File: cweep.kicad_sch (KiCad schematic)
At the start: 57 parts

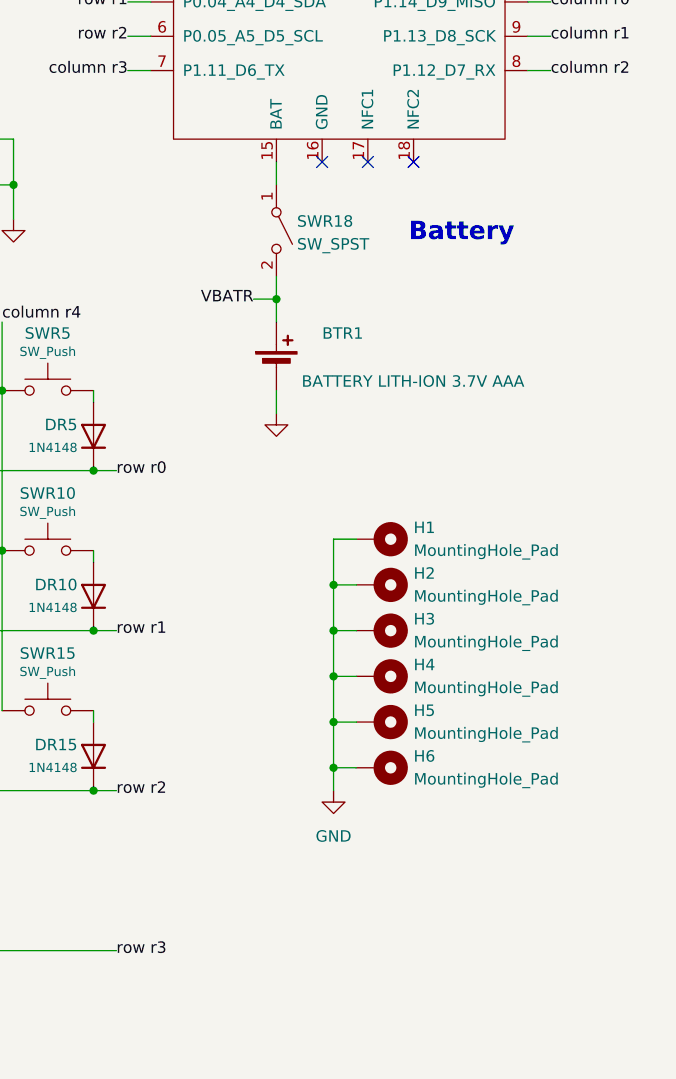
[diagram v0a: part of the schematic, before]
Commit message: refactor: reorganize battery schematic
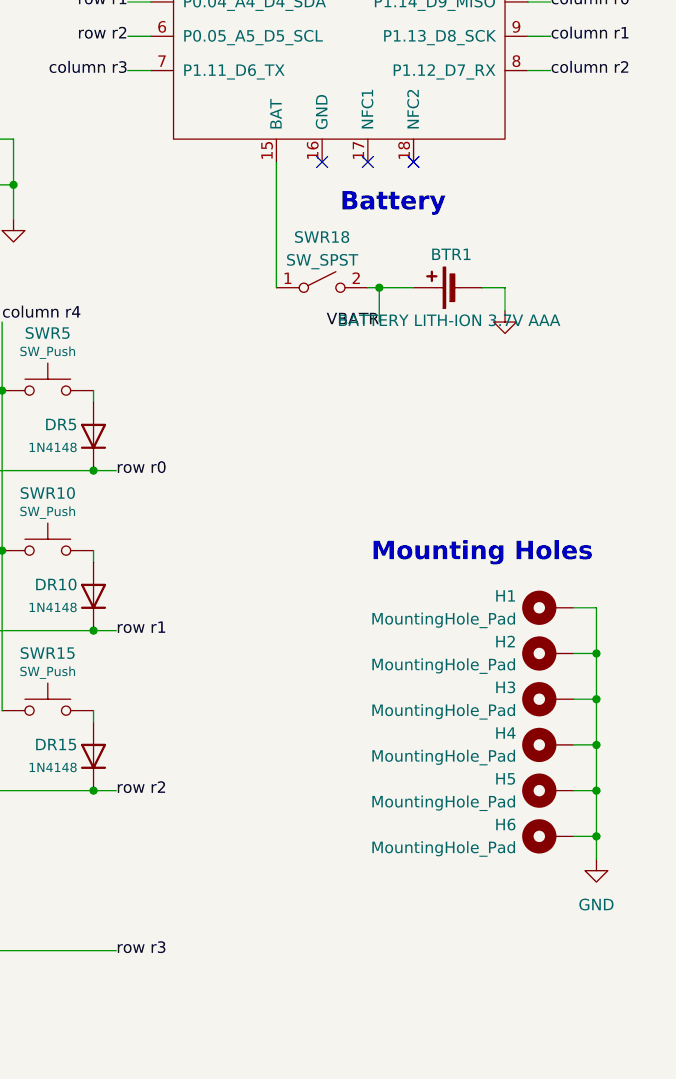
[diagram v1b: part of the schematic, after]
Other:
- note added: "Mounting Holes"
- moved on the sheet: BTR1, H1, H2, H3, H4, H5, H6, SWR18

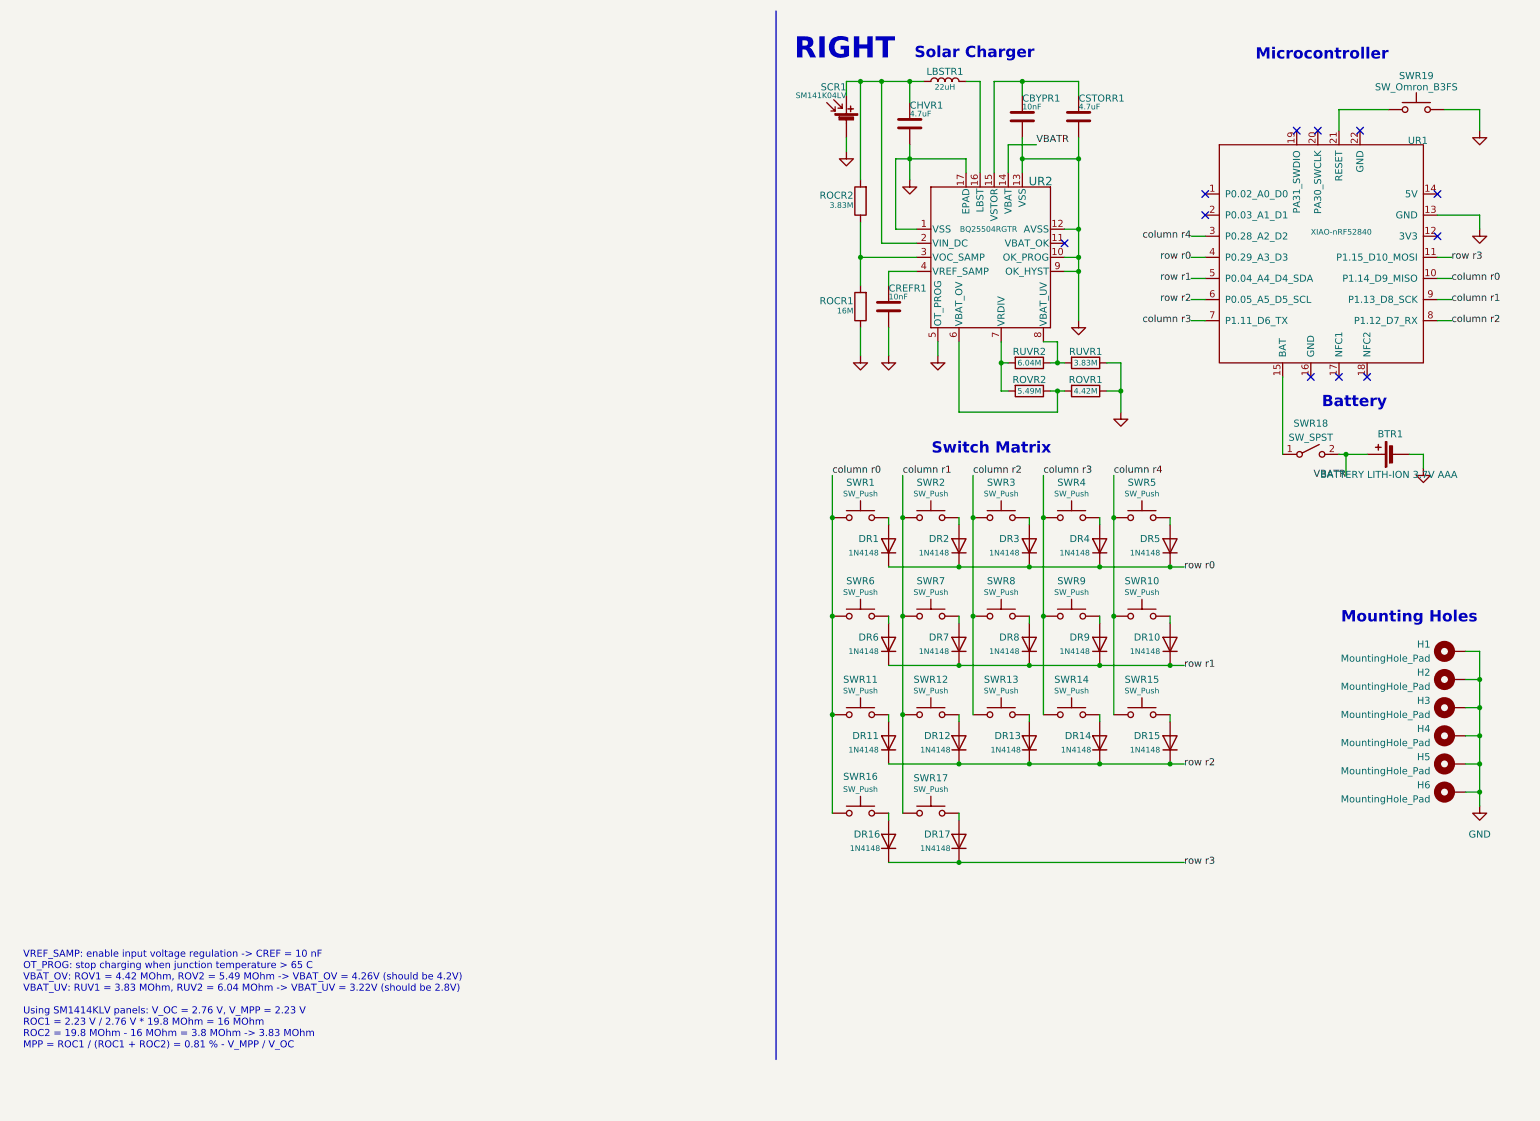
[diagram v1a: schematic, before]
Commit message: feat: add solar cell connectors
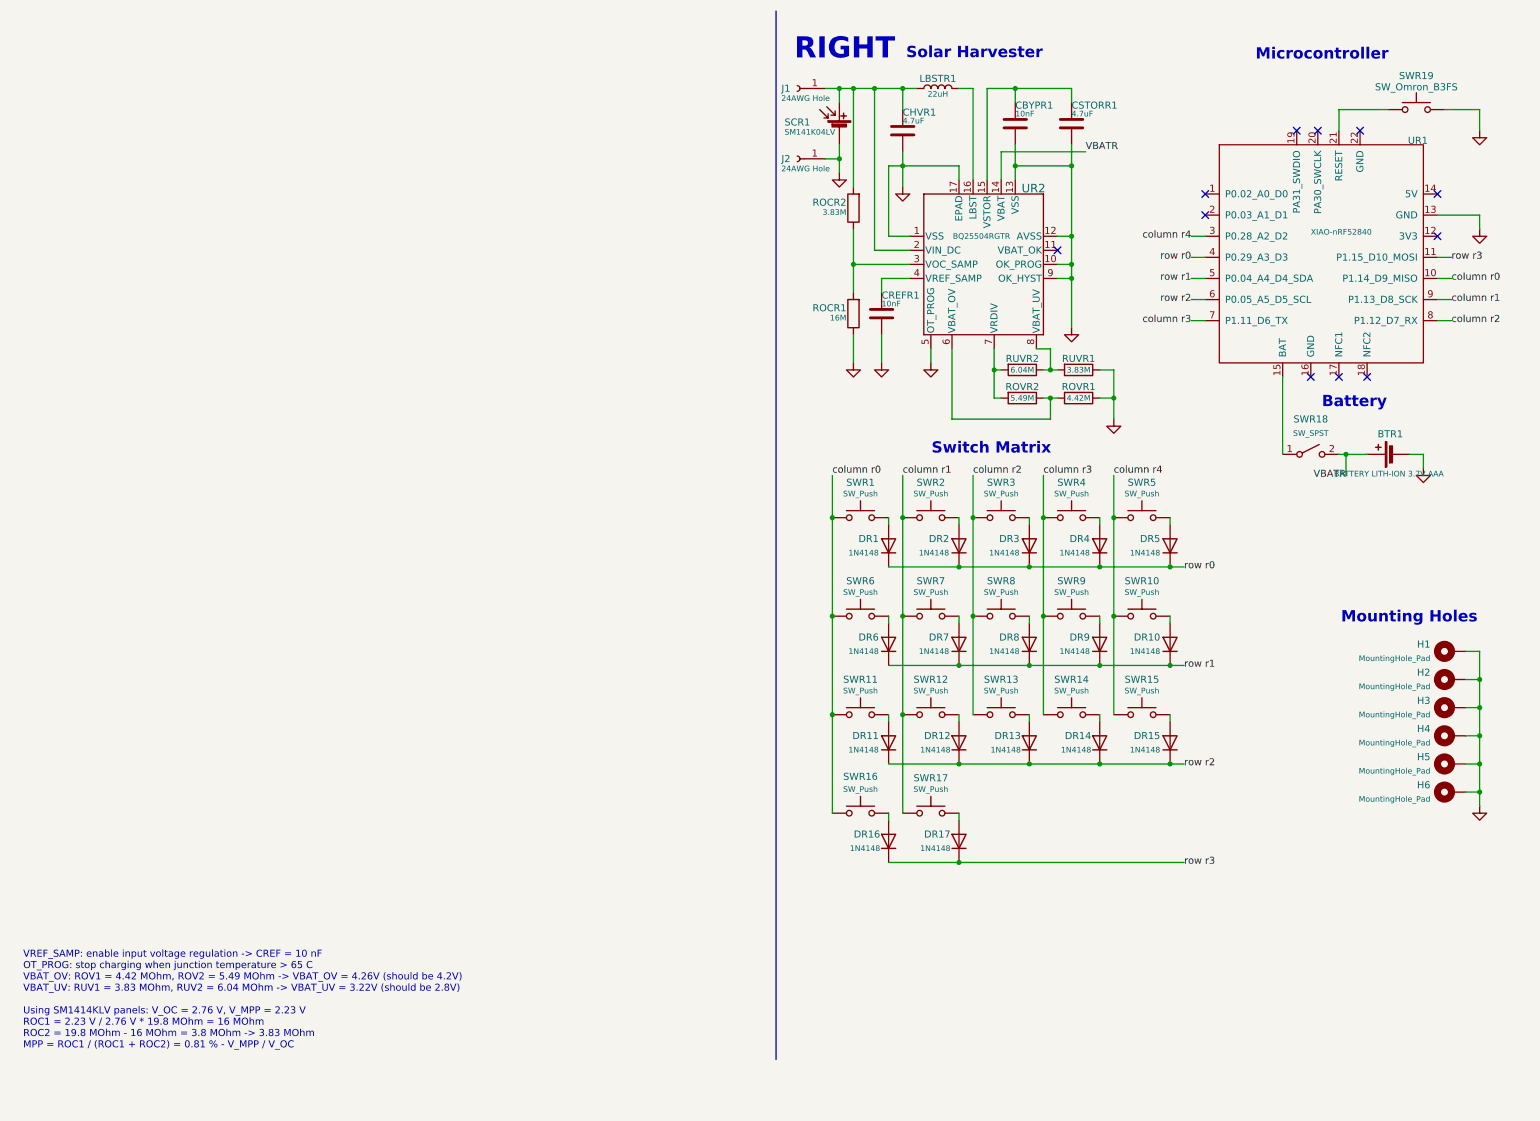
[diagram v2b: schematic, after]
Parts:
- added J1, J2: 24AWG Hole, Connector_Wire:SolderWire-0.127sqmm_1x01_D0.48mm_OD1mm_Relief, symbol Connector:Conn_01x01_Socket
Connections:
- net GND: now also J2.1 (Pin_1)
- net at CHVR1.1, LBSTR1.1, ROCR2.2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: now also J1.1 (Pin_1)
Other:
- note added: "Solar Harvester"
- note removed: "Solar Charger"
- moved on the sheet: CBYPR1, CHVR1, CREFR1, CSTORR1, LBSTR1, ROCR1, ROCR2, ROVR1, ROVR2, RUVR1, RUVR2, SCR1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

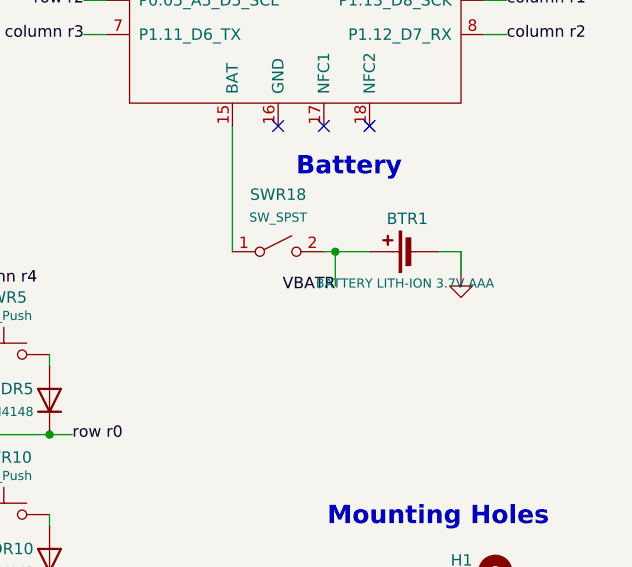
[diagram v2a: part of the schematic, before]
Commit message: fix: AAA -> 10440
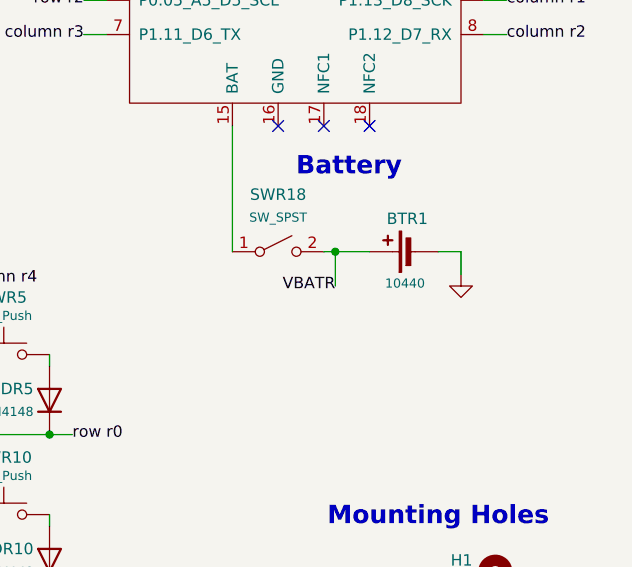
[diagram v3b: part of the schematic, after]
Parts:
- BTR1: value BATTERY LITH-ION 3.7V AAA -> 10440
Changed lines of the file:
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@@
 			)
 		)
-		(property "Value" "BATTERY\nLITH-ION\n3.7V\nAAA"
+		(property "Value" "10440"
 			(at 259.207 93.091 90)
 			(effects

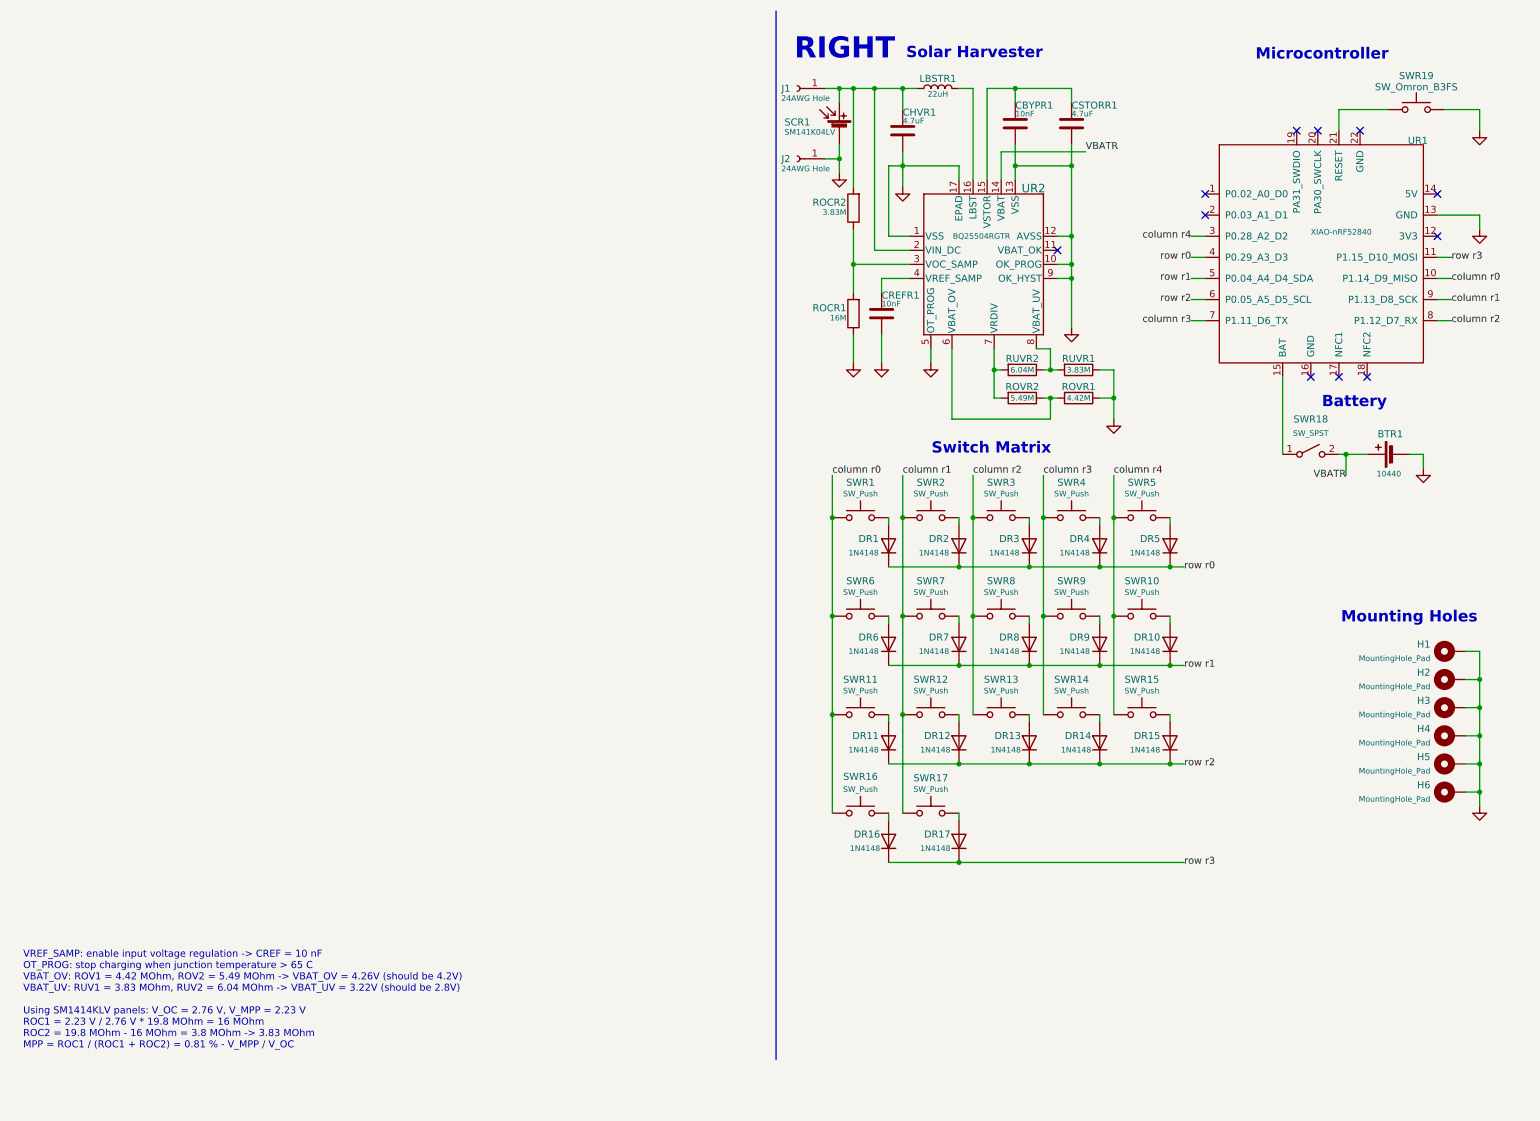
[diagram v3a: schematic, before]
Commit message: refactor: normalize labels and organize schematic
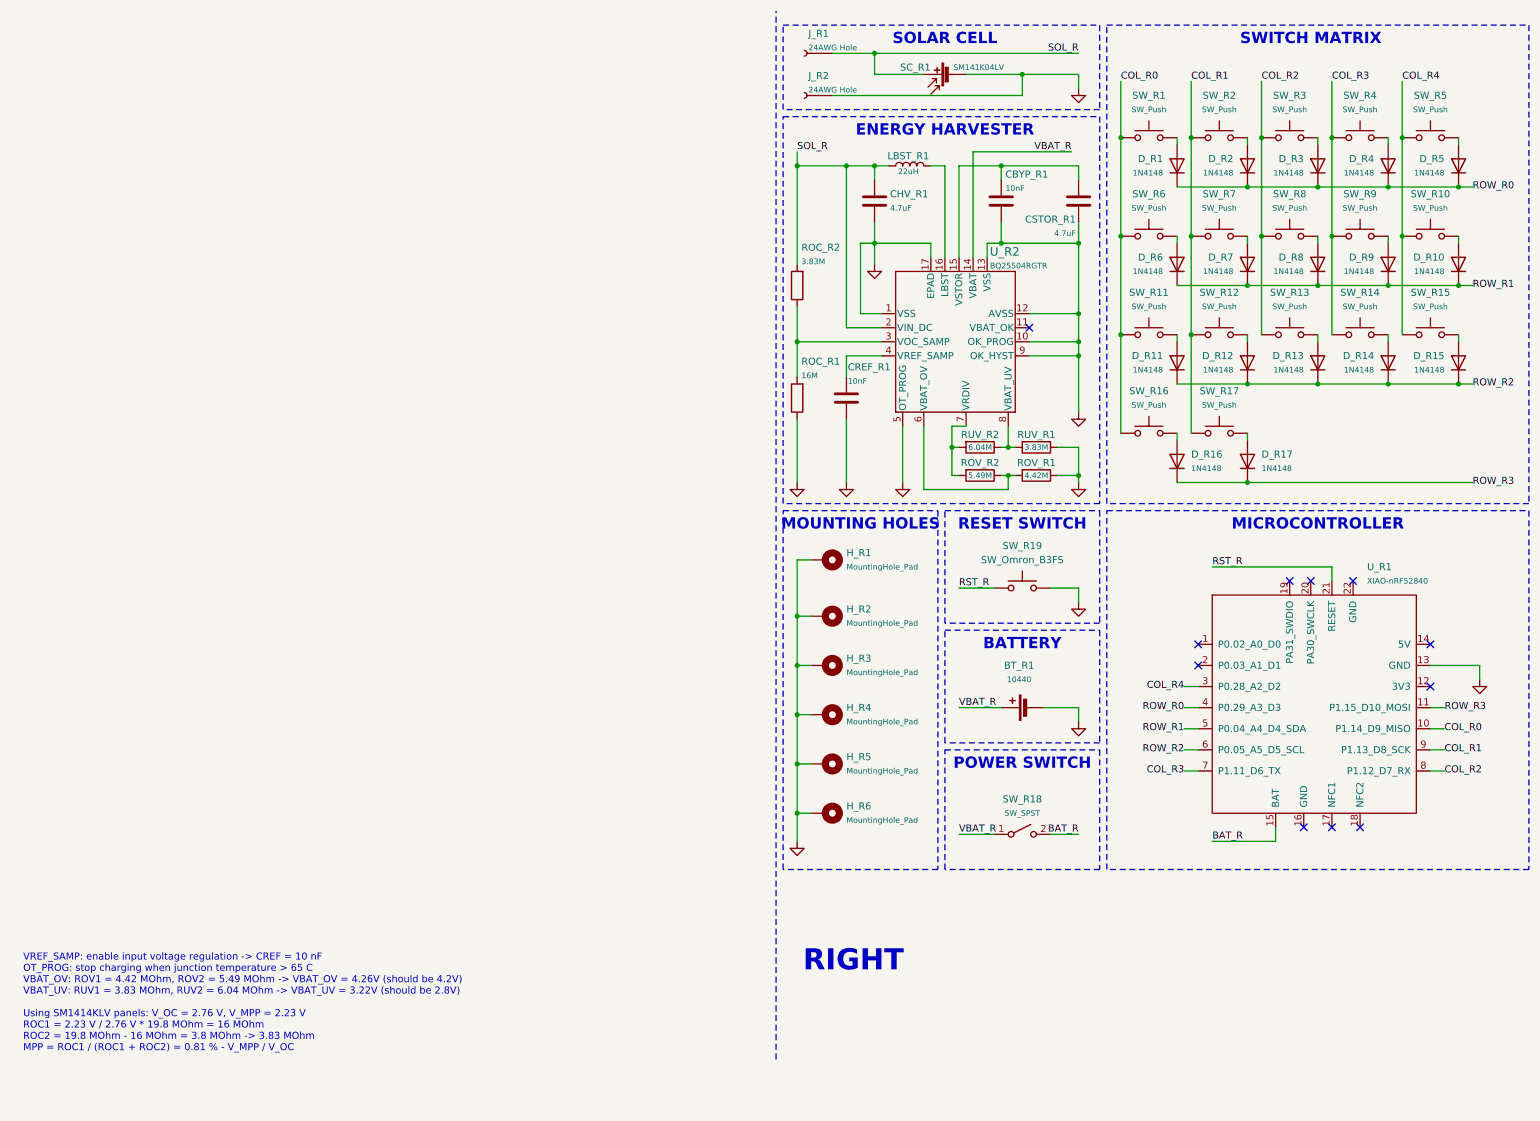
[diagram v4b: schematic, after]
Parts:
- BT_R1: renamed from BTR1; footprint com_snapeda_Keystone:BatteryHolder_Keystone_230-1_1xAAA -> com_snapeda_Keystone:BatteryHolder_Keystone_230-1_1x10440
- renumbered CBYPR1 to CBYP_R1, CHVR1 to CHV_R1, CREFR1 to CREF_R1, CSTORR1 to CSTOR_R1, DR1 to D_R1, DR10 to D_R10, DR11 to D_R11, DR12 to D_R12, DR13 to D_R13, DR14 to D_R14, DR15 to D_R15, DR16 to D_R16, DR17 to D_R17, DR2 to D_R2, DR3 to D_R3, DR4 to D_R4, DR5 to D_R5, DR6 to D_R6, DR7 to D_R7, DR8 to D_R8, DR9 to D_R9, H1 to H_R1, H2 to H_R2, H3 to H_R3, H4 to H_R4, H5 to H_R5, H6 to H_R6, J1 to J_R1, J2 to J_R2, LBSTR1 to LBST_R1, ROCR1 to ROC_R1, ROCR2 to ROC_R2, ROVR1 to ROV_R1, ROVR2 to ROV_R2, RUVR1 to RUV_R1, RUVR2 to RUV_R2, SCR1 to SC_R1, SWR1 to SW_R1, SWR10 to SW_R10, SWR11 to SW_R11, SWR12 to SW_R12, SWR13 to SW_R13, SWR14 to SW_R14, SWR15 to SW_R15, SWR16 to SW_R16, SWR17 to SW_R17, SWR18 to SW_R18, SWR19 to SW_R19, SWR2 to SW_R2, SWR3 to SW_R3, SWR4 to SW_R4, SWR5 to SW_R5, SWR6 to SW_R6, SWR7 to SW_R7, SWR8 to SW_R8, SWR9 to SW_R9, UR1 to U_R1, UR2 to U_R2
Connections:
- net SOL_R: now reaches CHV_R1.1, J_R1.1 (Pin_1), LBST_R1.1, ROC_R2.2, SC_R1.1 (+), U_R2.2 (VIN_DC)
- net BAT_R: now reaches U_R1.15 (BAT)
- net BAT_R: now also SW_R18.2 (B); no longer SW_R18.1 (A)
- net RST_R: now reaches SW_R19.1, U_R1.21 (RESET)
- net VBATR renamed VBAT_R
- net VBAT_R: now also SW_R18.1 (A); no longer SW_R18.2 (B)
- net column r0 renamed COL_R0
- net column r1 renamed COL_R1
- net column r2 renamed COL_R2
- net column r3 renamed COL_R3
- net column r4 renamed COL_R4
- net row r0 renamed ROW_R0
- net row r1 renamed ROW_R1
- net row r2 renamed ROW_R2
- net row r3 renamed ROW_R3
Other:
- note added: "BATTERY"
- note added: "ENERGY HARVESTER"
- note added: "MICROCONTROLLER"
- note added: "MOUNTING HOLES"
- note added: "POWER SWITCH"
- note added: "RESET SWITCH"
- note added: "SOLAR CELL"
- note added: "SWITCH MATRIX"
- note removed: "Battery"
- note removed: "Microcontroller"
- note removed: "Mounting Holes"
- note removed: "Solar Harvester"
- note removed: "Switch Matrix"
- moved on the sheet: BT_R1, CBYP_R1, CHV_R1, CREF_R1, CSTOR_R1, D_R1, D_R10, D_R11, D_R12, D_R13, D_R14, D_R15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
